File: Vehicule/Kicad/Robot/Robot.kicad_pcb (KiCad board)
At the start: 2 copper layers, 60 x 50 mm, 11 parts, among them J1 Conn_01x02_Socket, J2 Conn_01x02_Socket, J3 Conn_01x01_Socket, J4 Conn_01x01_Socket, J5 Conn_01x01_Socket, J6 Conn_01x01_Socket, U1 ESP32-C3_SUPERMINI, U2 L293D

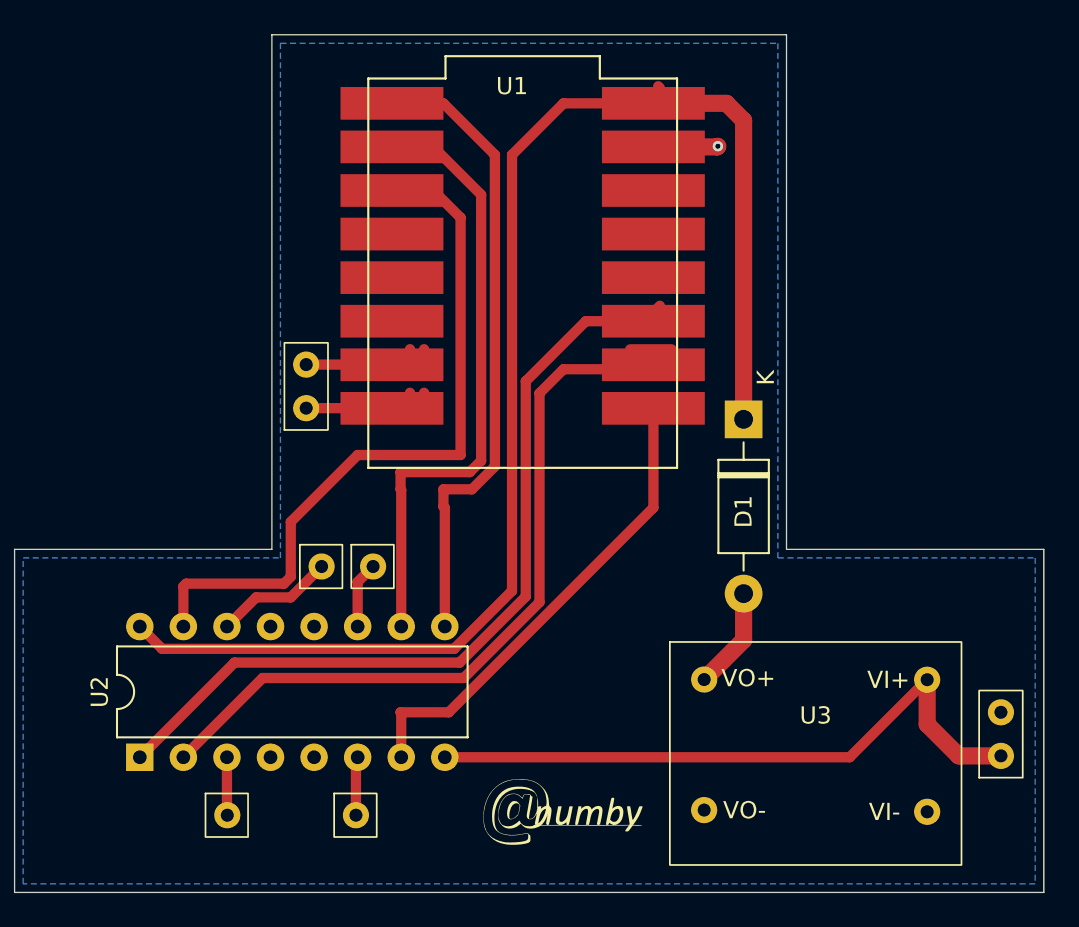
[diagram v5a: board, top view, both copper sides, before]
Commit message: Ajout de logo Anumby pour PCB Mise à jour des empreintes, des connecteurs des librairies
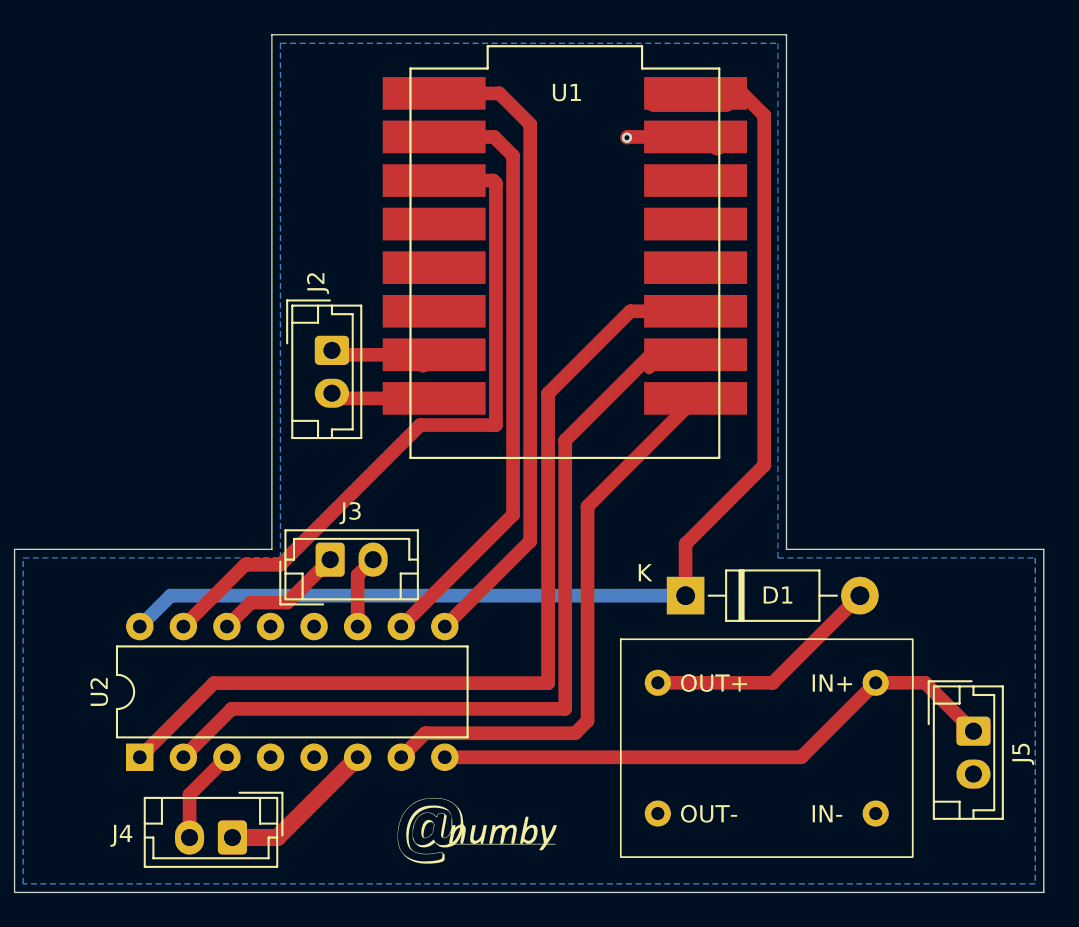
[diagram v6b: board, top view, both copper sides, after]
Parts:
- removed J1: Conn_01x02_Socket, Anumby:CONN-2-PINS
- removed J6: Conn_01x01_Socket, Anumby:CONN-1-PINS
- removed U3: ~, Anumby:Regulator-DFR0569
- added U4: REG_5V, Anumby:REG_5V_DFR, F.Cu at (116.0, 144.5)
- J2: value Conn_01x02_Socket -> Conn_01x02_Socket_H; footprint Anumby:CONN-2-PINS -> Connector_JST:JST_EH_B2B-EH-A_1x02_P2.50mm_Vertical
- J3, J4, J5: value Conn_01x01_Socket -> Conn_01x02_Socket_H; footprint Anumby:CONN-1-PINS -> Connector_JST:JST_EH_B2B-EH-A_1x02_P2.50mm_Vertical
- moved J5 35.1 mm to (128.0, 143.5), turned to -90 degrees
- moved J4 18.4 mm to (84.8, 149.7), turned to 180 degrees
- moved D1 10.8 mm to (111.2, 135.6), turned to 0 degrees
- moved G 5.12 mm to (99.1, 149.3)
- moved J2 2.58 mm to (90.6, 121.3), turned to -90 degrees
- moved U1 2.53 mm to (104.2, 116.3)
- moved J3 0.87 mm to (90.5, 133.5)
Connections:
- U1 pad 20: Net-(J2-Pin_2) -> Net-(J2-Pin_1)
- U1 pad 21: Net-(J2-Pin_1) -> Net-(J2-Pin_2)
- U2 pad 11: Net-(J4-Pin_1) -> Net-(J3-Pin_2)
- U2 pad 3: Net-(J6-Pin_1) -> Net-(J4-Pin_2)
- U2 pad 6: Net-(J5-Pin_1) -> Net-(J4-Pin_1)
- U2 pad 8: Net-(J1-Pin_1) -> Net-(J5-Pin_1)
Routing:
- net Net-(J1-Pin_1): track 37.7 -> 0.00 mm
- net Net-(J5-Pin_1): track 3.82 -> 33.8 mm
- net Net-(D1-K): track 81.8 -> 71.4 mm
- net Net-(D1-A): track 5.96 -> 13.9 mm
- net Net-(J4-Pin_2): track 0.00 -> 5.58 mm
- net Net-(J4-Pin_1): track 3.93 -> 9.24 mm
- net Net-(U1-GPIO2): track 48.1 -> 53.3 mm
- net Net-(U1-GPIO0): track 28.1 -> 33.1 mm
- net Net-(J3-Pin_2): track 0.00 -> 4.27 mm
- net Net-(U1-GPIO5): track 37.0 -> 40.7 mm
- net Net-(J6-Pin_1): track 3.39 -> 0.00 mm
- net Net-(U1-GPIO1): track 46.4 -> 49.1 mm
- net Net-(J2-Pin_1): track 5.03 -> 7.00 mm
- net Net-(U1-GPIO6): track 35.9 -> 37.6 mm
- net Net-(U1-GPIO7): track 42.0 -> 43.3 mm
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
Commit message: Finalisation du PCB du Robot puis génération des fichiers de fabrication Gerber
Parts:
- added SW1: SW_DPDT_x2, Button_Switch_THT:SW_Slide_SPDT_Straight_CK_OS102011MS2Q, F.Cu at (102.6, 149.3)
- moved G 30.2 mm to (126.2, 136.0)
- moved D1 2.10 mm to (109.1, 135.6)
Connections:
- U2 pad 8: Net-(J5-Pin_1) -> Net-(SW1A-B)
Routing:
- net Net-(SW1A-B): track 0.00 -> 5.70 mm
- net Net-(J5-Pin_1): track 33.8 -> 32.3 mm
- net Net-(D1-K): track 71.4 -> 70.2 mm
- net Net-(D1-A): track 13.9 -> 12.9 mm
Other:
- board text added: "ESP32-C3"
- board text added: "GND"
- board text added: "MOTOR DRIVER"
- board text added: "ON/OFF"
- board text added: "REGULATOR"
- board text added: "VCC"

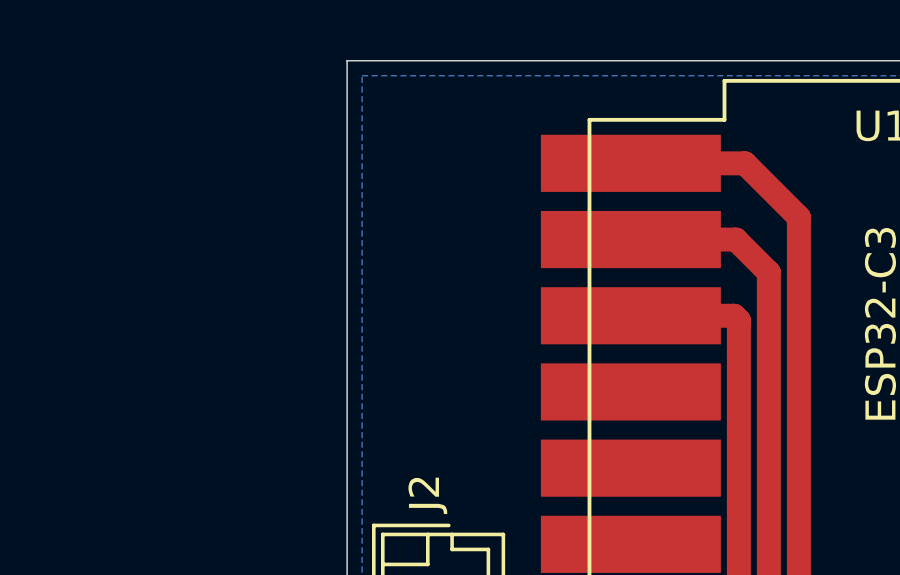
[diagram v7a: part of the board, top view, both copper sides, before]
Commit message: Ajout d'un titre ROBOT / TELECOMMANDE et d'une version (V1) sur la sérigraphie
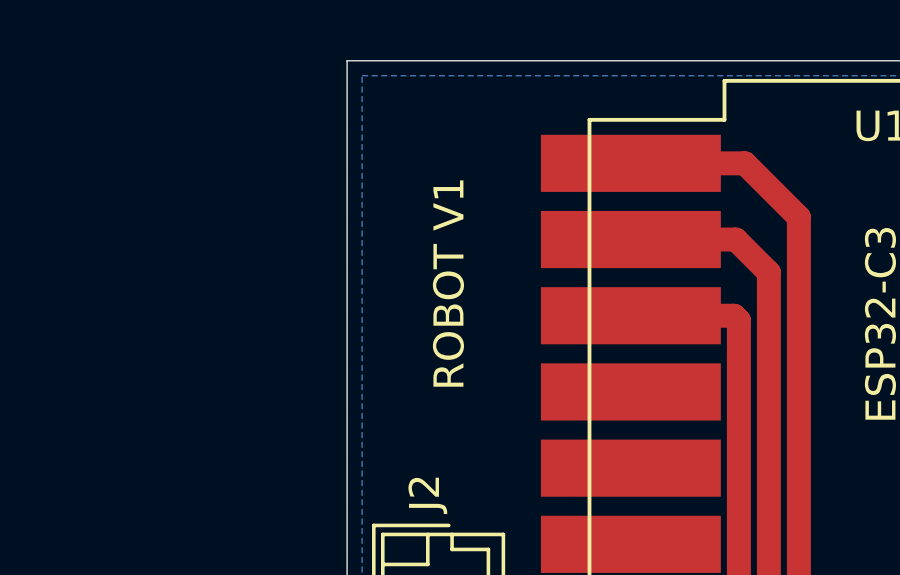
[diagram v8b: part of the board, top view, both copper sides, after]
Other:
- board text added: "ROBOT V1"
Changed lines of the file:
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@@
 		(tags "switch SPDT")
 		(property "Reference" "SW1"
-			(at 3.99 -2.99 360)
+			(at 3.99 -2.99 0)
 			(layer "F.SilkS")
 			(hide yes)
@@
 		)
 		(property "Value" "SW_DPDT_x2"
-			(at 2 3 360)
+			(at 2 3 0)
 			(layer "F.Fab")
 			(effects
@@
 		)
 		(fp_text user "${REFERENCE}"
-			(at 3.99 -2.99 360)
+			(at 3.99 -2.99 0)
 			(layer "F.Fab")
 			(effects
@@
 		(layer "F.SilkS")
 		(effects
+			(font
+				(size 1 1)
+				(thickness 0.1)
+			)
+			(justify left bottom)
+		)
+	)
+	(gr_text "ROBOT V1"
+		(at 91.1 113.934314 90)
+		(layer "F.SilkS")
+		(effects
